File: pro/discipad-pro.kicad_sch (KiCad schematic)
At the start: 63 parts, among them SW0 KEYSW, SW1 KEYSW, SW10 KEYSW, SW11 KEYSW, SW12 KEYSW, SW13 KEYSW, SW14 KEYSW, SW15 KEYSW, SW16 KEYSW, SW17 Rotary_Encoder_Switch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

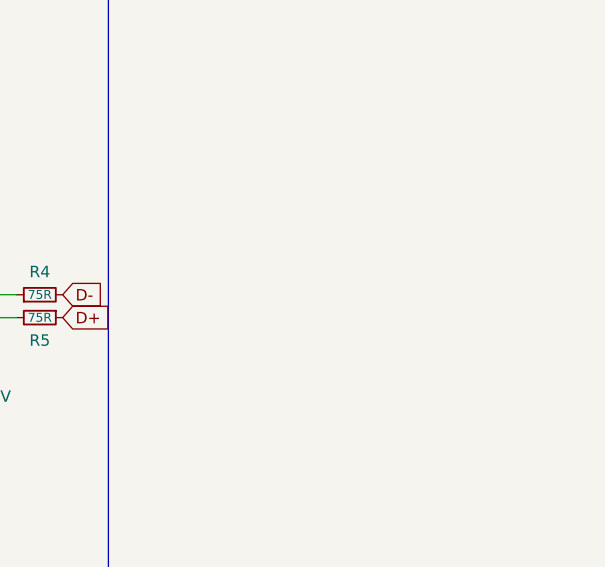
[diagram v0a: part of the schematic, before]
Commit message: Switch to USB-C and diode footprints from the 42. Keebs library
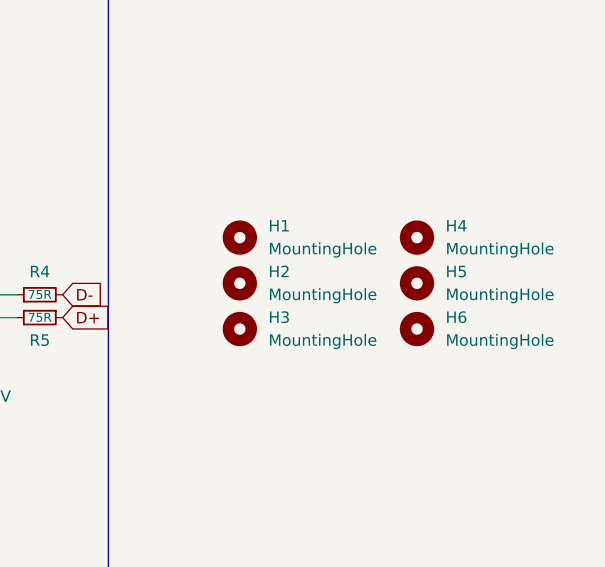
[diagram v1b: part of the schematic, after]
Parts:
- added H1, H2, H3, H4, H5, H6: MountingHole, MountingHole:MountingHole_2.2mm_M2_Pad, symbol Mechanical:MountingHole
- D1, D10, D11, D12, D13, D14, D15, D16, D17, D2, D20, D21, D22, D3, D4, D5, D6, D7, D8, D9: footprint discipad:D_DO-35_SOD27_P5.08mm_Horizontal -> 42keebs:D_DO-35_SOD27_P5.08mm_Horizontal
- D18, D19: footprint discipad:D_DO-35_SOD27_P5.08mm_Horizontal -> 42keebs:ZD_DO-35_SOD27_P5.08mm_Horizontal_smaller
- USB1: footprint Type-C:USB_C_GCT_USB4085 -> 42keebs:USB_C_GCT_USB4085-offset-pads
